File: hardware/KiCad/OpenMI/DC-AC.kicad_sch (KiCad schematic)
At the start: 53 parts, among them Q2 IPL60R125P7, Q3 IPL60R125P7, U1 IRS2304S, U6 ACS722xLCTR-05AB, U8 MCP6002-SN

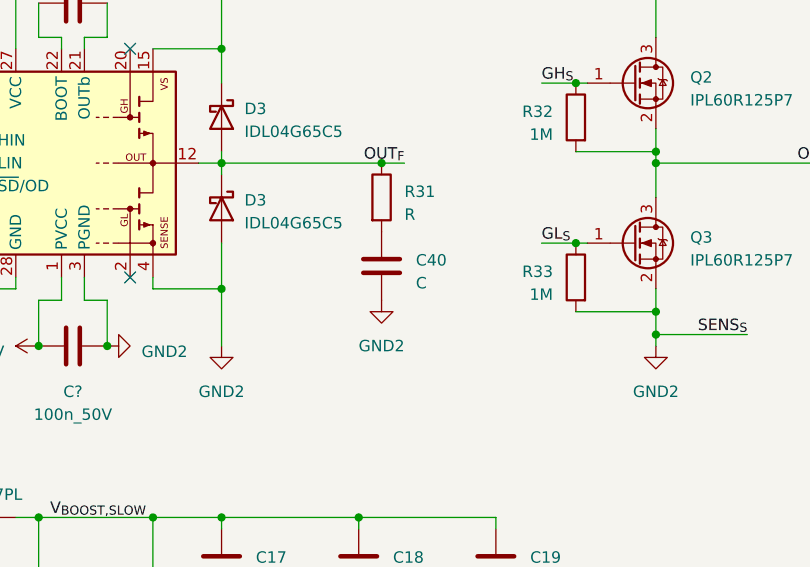
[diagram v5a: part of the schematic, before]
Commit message: feat(hw): Adds RC-Filter with `1206` footprint to MASTERGAN. Values are TBD.
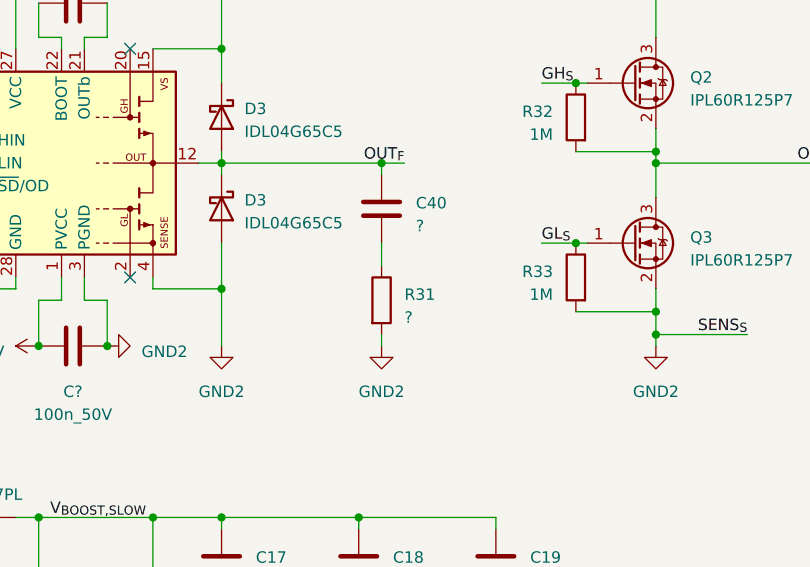
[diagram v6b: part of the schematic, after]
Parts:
- removed C40: C, symbol Device:C
- removed R31: R, symbol Device:R
- added C40: ?, Capacitor_SMD:C_1206_3216Metric, symbol _C_1206:?
- added R31: ?, Resistor_SMD:R_1206_3216Metric, symbol _R_1206:?
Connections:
- net GND: now also R31.2
- net OUT_{F}: now also C40.1
- new net: C40.2, R31.1

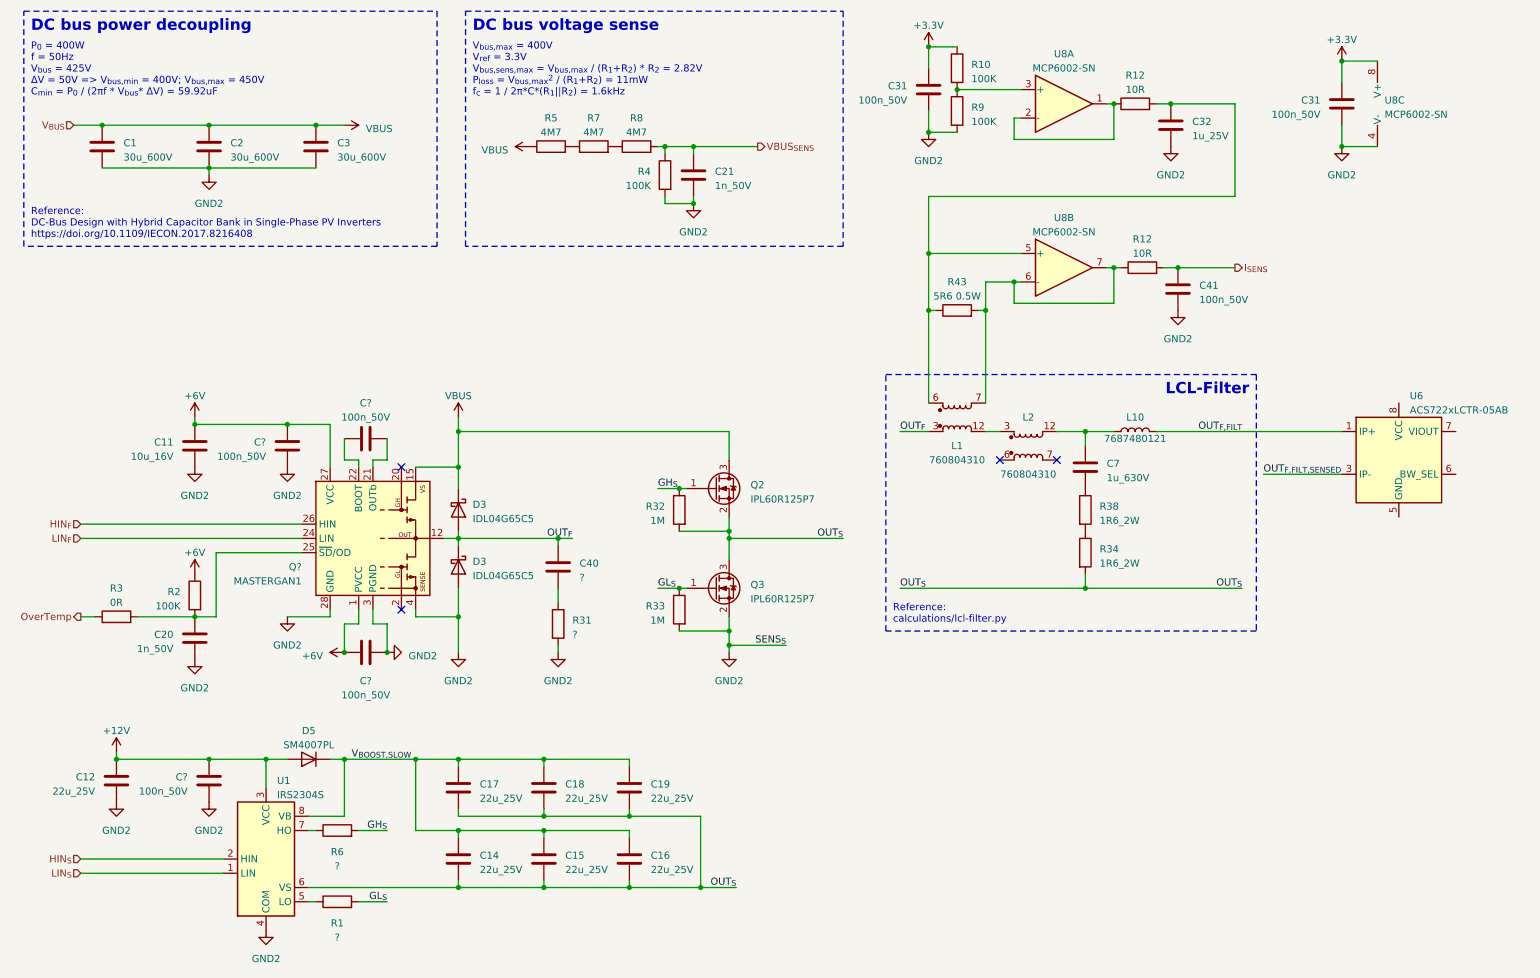
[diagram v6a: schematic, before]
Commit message: feat(hw): finishes inverter filter for now.
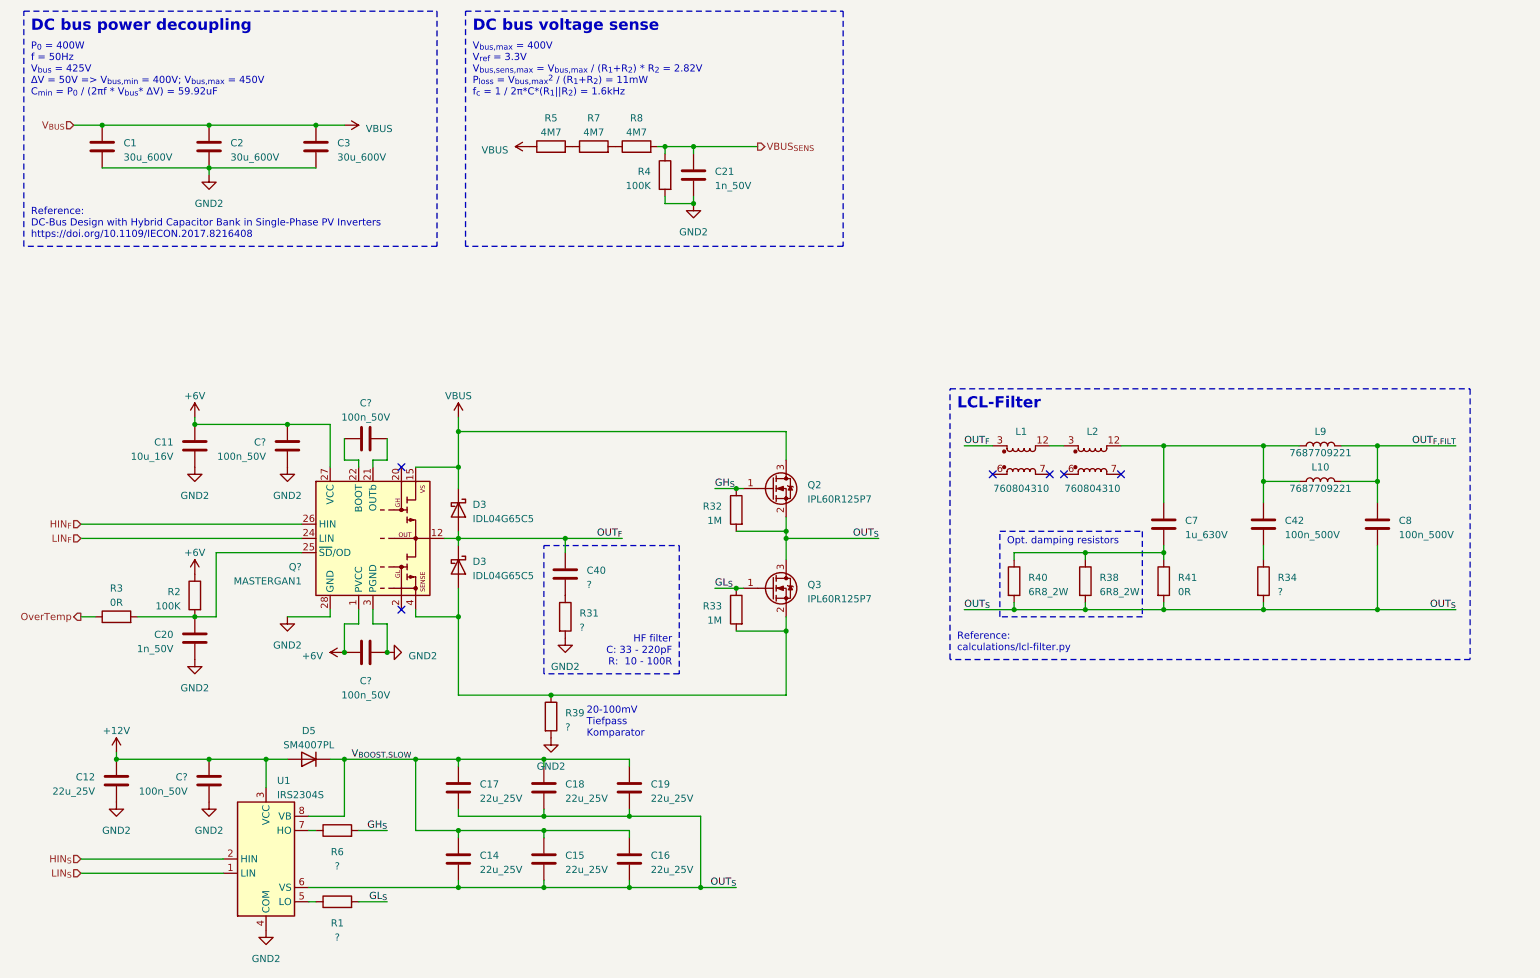
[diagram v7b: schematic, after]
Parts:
- removed C31 (x2), C41: 100n_50V, Capacitor_SMD:C_0603_1608Metric, symbol _C_0603:100n_50V
- removed C32: 1u_25V, Capacitor_SMD:C_0805_2012Metric, symbol _C_0805:1u_25V
- removed L10: 7687480121, OpenCE:L_Radial_D10.0mm_P5.00mm_H14.0mm_Wuerth_1014, symbol _L_Power:7687480121
- removed R10, R9: 100K, Resistor_SMD:R_0603_1608Metric, symbol _R_0603:100K
- removed R12 (x2): 10R, Resistor_SMD:R_0603_1608Metric, symbol _R_0603:10R
- removed R34, R38: 1R6_2W, Resistor_THT:R_Axial_DIN0411_L9.9mm_D3.6mm_P5.08mm_Vertical, symbol _R_Power:1R6_2W
- removed R43: 5R6 0.5W, symbol Device:R
- removed U6: ACS722xLCTR-05AB, Package_SO:SOIC-8_3.9x4.9mm_P1.27mm, symbol Sensor_Current:ACS722xLCTR-05AB
- removed U8: MCP6002-SN, Package_SO:SOIC-8_3.9x4.9mm_P1.27mm, symbol _Amplifier_Operational:MCP6002-SN
- added C42, C8: 100n_500V, Capacitor_SMD:C_1210_3225Metric, symbol _C_1210:100n_500V
- added L10, L9: 7687709221, OpenCE:L_Wuerth_WE-PD-1210, symbol _L_Power:7687709221
- added R34, R39: ?, Resistor_SMD:R_1206_3216Metric, symbol _R_1206:?
- added R38, R40: 6R8_2W, Resistor_THT:R_Axial_DIN0411_L9.9mm_D3.6mm_P5.08mm_Vertical, symbol _R_Power:6R8_2W
- added R41: 0R, Resistor_SMD:R_1206_3216Metric, symbol _R_1206:0R
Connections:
- net GND: now also R39.2; no longer D3.2 (A), Q3.2 (S), Q?.10 (SENSE), Q?.11 (SENSE), Q?.4, Q?.5 (SENSE), Q?.6 (SENSE), Q?.7 (SENSE), Q?.8 (SENSE), Q?.9 (SENSE), Q?.EP2 (SENSE), R33.2
- net OUT_{F,FILT}: now also C8.1, L10.2, L9.2
- net OUT_{S}: now also C8.2, R34.2, R38.2, R40.2, R41.2
- net at C7.1, L2.12: now also C42.1, L10.1, L9.1
- net at C7.2: now also R38.1, R40.1, R41.1
- new net: D3.2 (A), Q3.2 (S), Q?.10 (SENSE), Q?.11 (SENSE), Q?.4, Q?.5 (SENSE), Q?.6 (SENSE), Q?.7 (SENSE), Q?.8 (SENSE), Q?.9 (SENSE), Q?.EP2 (SENSE), R33.2, R39.1
- new net: C42.2, R34.1
- no-connect marks 4 -> 6
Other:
- note added: "20-100mV Tiefpass Komparator"
- note added: "HF filter C: 33 - 220pF R: 10 - 100R"
- note added: "Opt. damping resistors"
- moved on the sheet: C40, C7, L1, L2, Q2, Q3, R31, R32, R33

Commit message: feat(hw): Adds inverter current sensing
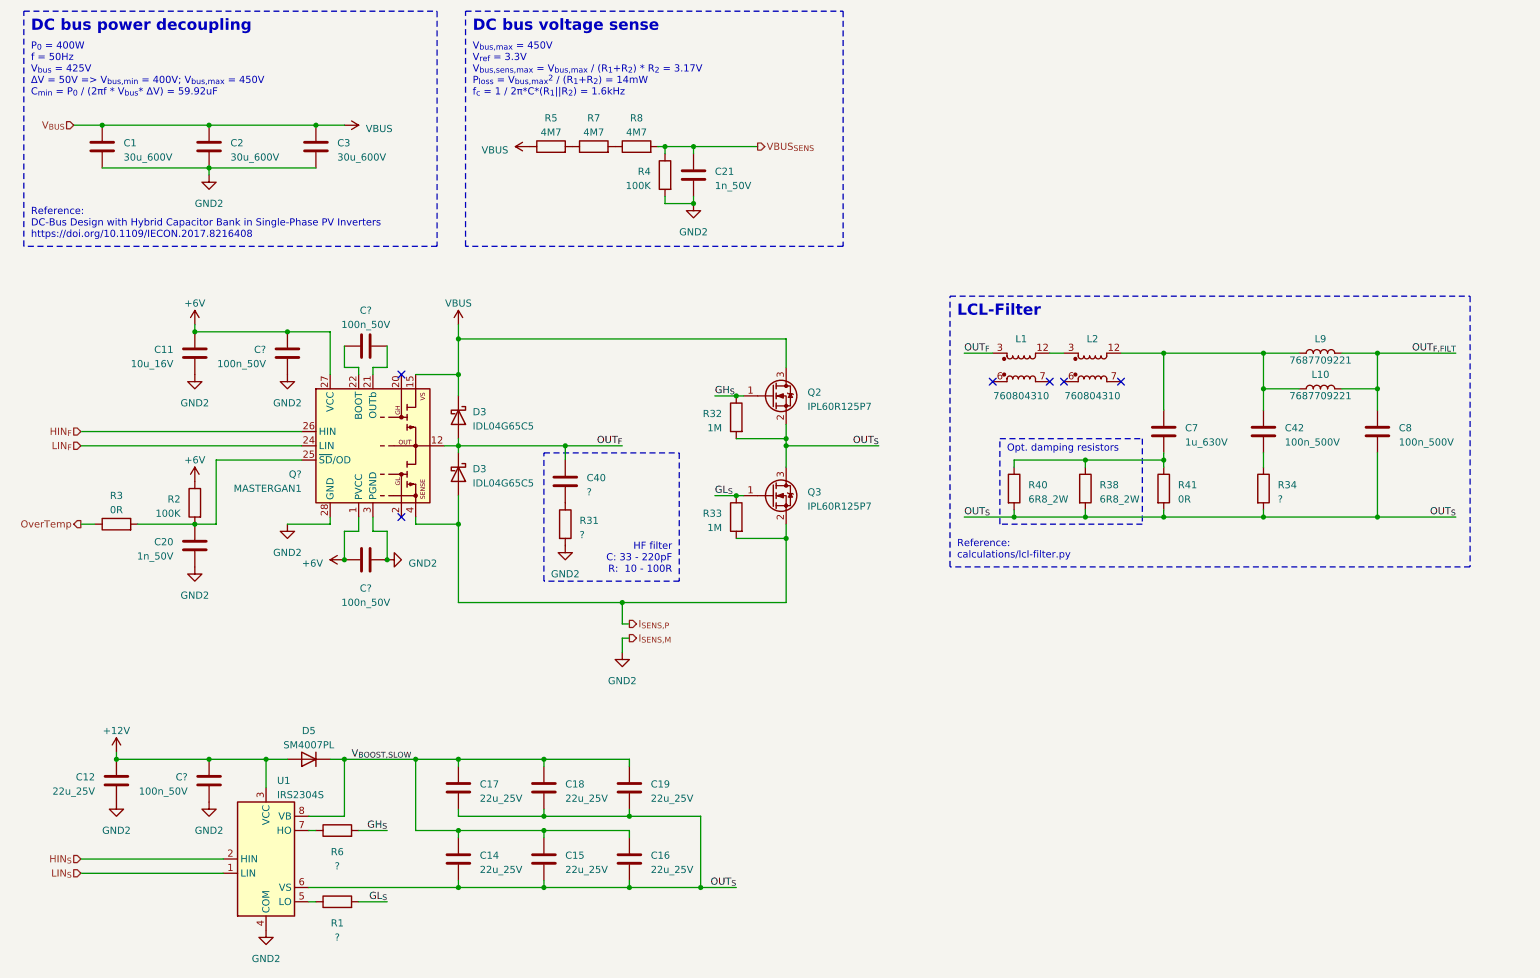
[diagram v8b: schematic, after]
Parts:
- removed R39: ?, Resistor_SMD:R_1206_3216Metric, symbol _R_1206:?
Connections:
- net I_{SENS,P}: now reaches D3.2 (A), Q3.2 (S), Q?.10 (SENSE), Q?.11 (SENSE), Q?.4, Q?.5 (SENSE), Q?.6 (SENSE), Q?.7 (SENSE), Q?.8 (SENSE), Q?.9 (SENSE), Q?.EP2 (SENSE), R33.2
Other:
- note added: "V_{bus,max} = 450V V_{ref} = 3.3V V_{bus,sens,max} = V_{bus,max} / (R_{1}+R_{2}) * R_{2} = 3.17V P_{loss} = V_{bus,max}^{2} / (R_{1}+R_{2}) = 14mW f_{c} = 1 / 2π*C*(R_{1}||R_{2}) = 1.6kHz"
- note removed: "20-100mV Tiefpass Komparator"
- note removed: "V_{bus,max} = 400V V_{ref} = 3.3V V_{bus,sens,max} = V_{bus,max} / (R_{1}+R_{2}) * R_{2} = 2.82V P_{loss} = V_{bus,max}^{2} / (R_{1}+R_{2}) = 11mW f_{c} = 1 / 2π*C*(R_{1}||R_{2}) = 1.6kHz"
- moved on the sheet: C11, C20, C40, C42, C7, C8, C?, D3, L1, L10, L2, L9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
